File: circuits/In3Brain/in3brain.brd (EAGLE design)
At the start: 107.4 x 51 mm, 35 parts, among them IC3 ATMEGA48/88/168-AU, IC4 REG1117, SW1 EC12E_SW

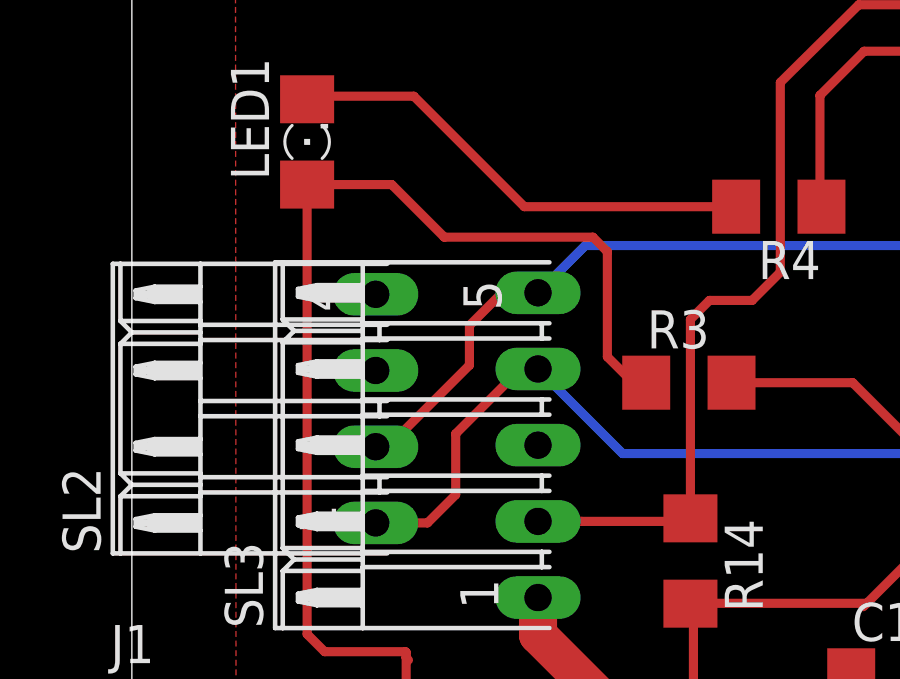
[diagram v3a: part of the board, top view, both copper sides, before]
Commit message: Circuit error fix & improved temperature selector
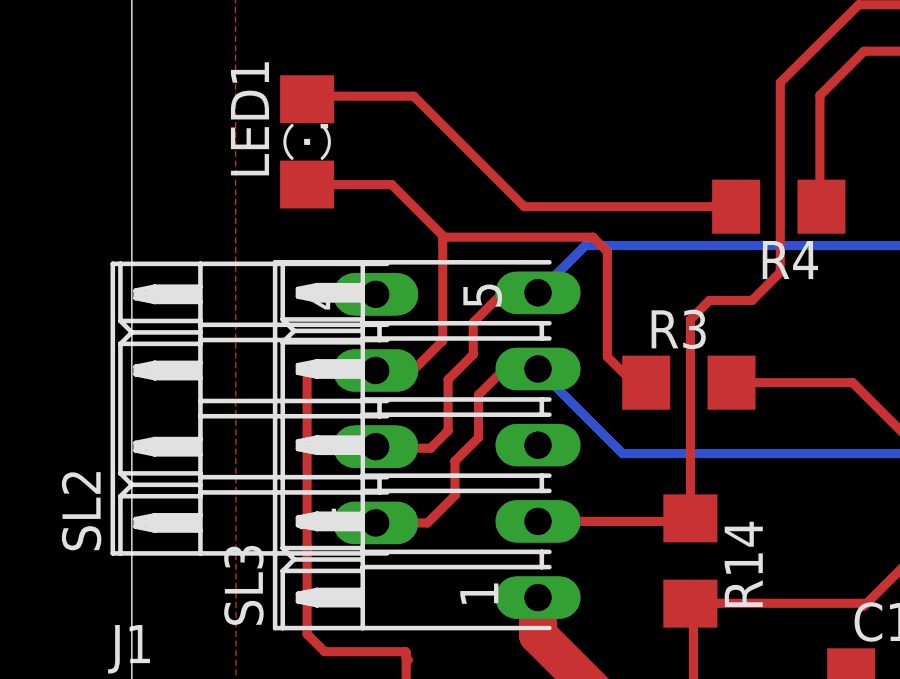
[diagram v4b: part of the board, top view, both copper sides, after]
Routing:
- net SDA: track 53.9 -> 55.8 mm
- net SCL: track 74.0 -> 74.9 mm
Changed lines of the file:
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@@
 <?xml version="1.0" encoding="utf-8"?>
 <!DOCTYPE eagle SYSTEM "eagle.dtd">
-<eagle version="8.0.1">
+<eagle version="8.0.0">
 <drawing>
 <settings>
@@
 <layers>
 <layer number="1" name="Top" color="4" fill="1" visible="yes" active="yes"/>
-<layer number="16" name="Bottom" color="1" fill="1" visible="no" active="yes"/>
+<layer number="16" name="Bottom" color="1" fill="1" visible="yes" active="yes"/>
 <layer number="17" name="Pads" color="2" fill="1" visible="yes" active="yes"/>
 <layer number="18" name="Vias" color="2" fill="1" visible="yes" active="yes"/>
@@
 <layer number="27" name="tValues" color="7" fill="1" visible="yes" active="yes"/>
 <layer number="28" name="bValues" color="7" fill="1" visible="yes" active="yes"/>
-<layer number="29" name="tStop" color="7" fill="3" visible="yes" active="yes"/>
+<layer number="29" name="tStop" color="7" fill="3" visible="no" active="yes"/>
 <layer number="30" name="bStop" color="7" fill="6" visible="yes" active="yes"/>
 <layer number="31" name="tCream" color="7" fill="4" visible="yes" active="yes"/>
@@
 <contactref element="SL4" pad="7"/>
 <wire x1="64.77" y1="33.274" x2="61.4426" y2="38.6838" width="0" layer="19" extent="1-1"/>
+<wire x1="13.7922" y1="26.9748" x2="8.382" y2="32.004" width="0" layer="19" extent="1-1"/>
 <wire x1="42.3164" y1="25.254" x2="50.6476" y2="26.054" width="0" layer="19" extent="1-1"/>
 <wire x1="32.2072" y1="29.9462" x2="32.2072" y2="27.1022" width="0" layer="19" extent="1-1"/>
-<wire x1="13.7922" y1="26.9748" x2="21.2598" y2="17.7546" width="0" layer="19" extent="1-1"/>
-<wire x1="8.382" y1="32.004" x2="13.7922" y2="26.9748" width="0" layer="19" extent="1-1"/>
 </signal>
 <signal name="5V">
@@
 <wire x1="96.8756" y1="9.9314" x2="22.7838" y2="9.9314" width="0.3048" layer="1"/>
 <wire x1="22.7838" y1="9.9314" x2="22.1488" y2="9.2964" width="0.3048" layer="1"/>
-<wire x1="6.096" y1="35.662" x2="6.096" y2="29.4386" width="0.3048" layer="1"/>
 <wire x1="6.096" y1="29.4386" x2="6.096" y2="20.6756" width="0.3048" layer="1"/>
 <wire x1="6.096" y1="20.6756" x2="6.6802" y2="20.0914" width="0.3048" layer="1"/>
 <wire x1="6.6802" y1="20.0914" x2="9.3726" y2="20.0914" width="0.3048" layer="1"/>
 <wire x1="9.3726" y1="20.0914" x2="9.398" y2="20.066" width="0.3048" layer="1"/>
-<wire x1="8.382" y1="29.464" x2="6.1214" y2="29.464" width="0.3048" layer="1"/>
+<wire x1="6.1214" y1="29.464" x2="8.382" y2="29.464" width="0.3048" layer="1"/>
 <wire x1="6.1214" y1="29.464" x2="6.096" y2="29.4386" width="0.3048" layer="1"/>
 <wire x1="9.4742" y1="19.812" x2="9.398" y2="19.8882" width="0.3048" layer="1"/>
@@
 <wire x1="16.1036" y1="29.9212" x2="16.1036" y2="33.4264" width="0.3048" layer="1"/>
 <wire x1="16.1036" y1="33.4264" x2="15.621" y2="33.909" width="0.3048" layer="1"/>
-<wire x1="15.621" y1="33.909" x2="10.668" y2="33.909" width="0.3048" layer="1"/>
+<wire x1="10.668" y1="33.909" x2="15.621" y2="33.909" width="0.3048" layer="1"/>
 <wire x1="10.668" y1="33.909" x2="8.9154" y2="35.6616" width="0.3048" layer="1"/>
 <wire x1="8.9154" y1="35.6616" x2="6.0964" y2="35.6616" width="0.3048" layer="1"/>
@@
 <wire x1="22.1488" y1="9.2964" x2="13.9954" y2="9.2964" width="0.3048" layer="1"/>
 <wire x1="13.9954" y1="9.2964" x2="9.398" y2="13.8938" width="0.3048" layer="1"/>
+<wire x1="10.668" y1="33.909" x2="10.6172" y2="33.909" width="0.3048" layer="1"/>
+<wire x1="8.382" y1="29.464" x2="9.6266" y2="29.464" width="0.3048" layer="1"/>
+<wire x1="10.6172" y1="30.4546" x2="10.6172" y2="33.8582" width="0.3048" layer="1"/>
+<wire x1="10.6172" y1="33.8582" x2="10.668" y2="33.909" width="0.3048" layer="1"/>
+<wire x1="9.6266" y1="29.464" x2="10.6172" y2="30.4546" width="0.3048" layer="1"/>
 <wire x1="58.8518" y1="35.789" x2="58.0644" y2="36.8304" width="0" layer="19" extent="1-1"/>
 <wire x1="20.2434" y1="29.0576" x2="17.3994" y2="29.0576" width="0" layer="19" extent="1-1"/>
@@
 <contactref element="SL3" pad="5"/>
 <wire x1="8.382" y1="26.924" x2="8.7884" y2="26.924" width="0.3048" layer="1"/>
-<wire x1="8.7884" y1="26.924" x2="11.5062" y2="29.6418" width="0.3048" layer="1"/>
-<wire x1="11.5062" y1="29.6418" x2="11.5062" y2="30.9626" width="0.3048" layer="1"/>
-<wire x1="11.5062" y1="30.9626" x2="12.7" y2="32.1564" width="0.3048" layer="1"/>
 <wire x1="12.7" y1="32.1564" x2="13.6906" y2="32.1564" width="0.3048" layer="1"/>
 <wire x1="13.6906" y1="32.1564" x2="13.7922" y2="32.0548" width="0.3048" layer="1"/>
@@
 <wire x1="49.4792" y1="34.4678" x2="49.4792" y2="35.8394" width="0.3048" layer="1"/>
 <wire x1="49.4792" y1="35.8394" x2="49.5046" y2="35.8648" width="0.3048" layer="1"/>
+<wire x1="13.7922" y1="32.0548" x2="12.6238" y2="32.0548" width="0.3048" layer="1"/>
+<wire x1="12.6238" y1="32.0548" x2="11.6332" y2="31.0642" width="0.3048" layer="1"/>
+<wire x1="11.6332" y1="31.0642" x2="11.6332" y2="29.9974" width="0.3048" layer="1"/>
+<wire x1="11.6332" y1="29.9974" x2="10.795" y2="29.1592" width="0.3048" layer="1"/>
+<wire x1="10.795" y1="29.1592" x2="10.795" y2="27.4574" width="0.3048" layer="1"/>
+<wire x1="10.795" y1="27.4574" x2="10.2108" y2="26.8732" width="0.3048" layer="1"/>
+<wire x1="10.2108" y1="26.8732" x2="8.9408" y2="26.8732" width="0.3048" layer="1"/>
+<wire x1="8.9408" y1="26.8732" x2="8.89" y2="26.924" width="0.3048" layer="1"/>
 </signal>
 <signal name="SCL">
@@
 <via x="52.578" y="35.3822" extent="1-16" drill="0.6" shape="square"/>
 <contactref element="SL3" pad="4"/>
-<wire x1="13.7922" y1="29.5148" x2="13.208" y2="29.5148" width="0.3048" layer="1"/>
-<wire x1="13.208" y1="29.5148" x2="11.049" y2="27.3558" width="0.3048" layer="1"/>
-<wire x1="11.049" y1="27.3558" x2="11.049" y2="25.3238" width="0.3048" layer="1"/>
+<wire x1="13.208" y1="29.5148" x2="13.7922" y2="29.5148" width="0.3048" layer="1"/>
 <wire x1="11.049" y1="25.3238" x2="10.1092" y2="24.384" width="0.3048" layer="1"/>
 <wire x1="10.1092" y1="24.384" x2="8.382" y2="24.384" width="0.3048" layer="1"/>
@@
 <wire x1="53.1876" y1="30.5058" x2="53.1876" y2="35.3568" width="0.3048" layer="1"/>
 <wire x1="53.1876" y1="35.3568" x2="52.578" y2="35.3822" width="0.3048" layer="1"/>
+<wire x1="13.7922" y1="29.5148" x2="12.6746" y2="29.5148" width="0.3048" layer="1"/>
+<wire x1="12.6746" y1="29.5148" x2="11.811" y2="28.6512" width="0.3048" layer="1"/>
+<wire x1="11.811" y1="28.6512" x2="11.811" y2="27.2288" width="0.3048" layer="1"/>
+<wire x1="11.811" y1="27.2288" x2="11.0236" y2="26.4414" width="0.3048" layer="1"/>
+<wire x1="11.0236" y1="26.4414" x2="11.0236" y2="25.3492" width="0.3048" layer="1"/>
+<wire x1="11.0236" y1="25.3492" x2="11.049" y2="25.3238" width="0.3048" layer="1"/>
 </signal>
 <signal name="N$1">
